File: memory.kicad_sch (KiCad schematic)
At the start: 4 parts, among them U8 62256, U9 KM28C64A

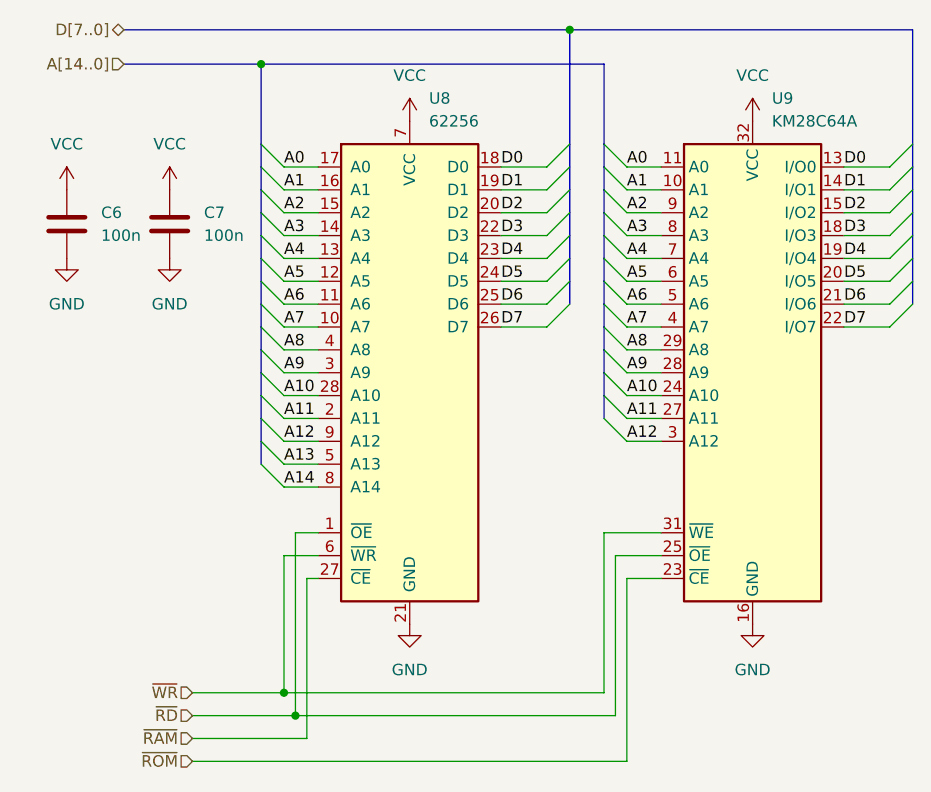
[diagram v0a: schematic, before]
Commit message: HW: Initial placement of I/O chips
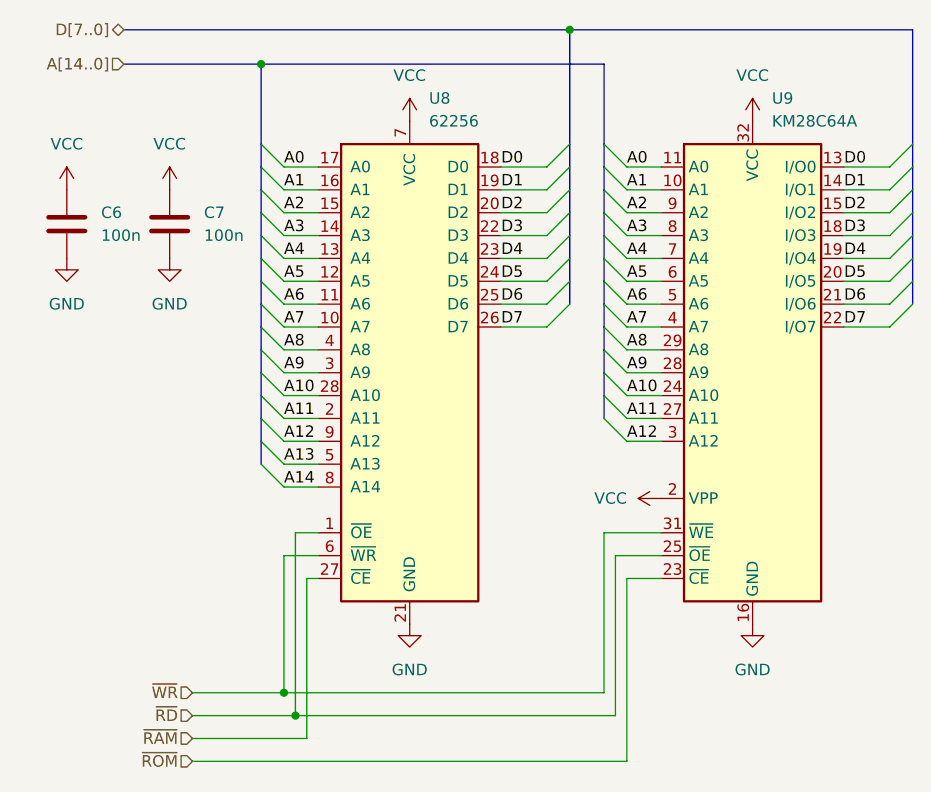
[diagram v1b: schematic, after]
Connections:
- net VCC: now also U9.2 (VPP)
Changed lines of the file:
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@@
+	)
+	(symbol
+		(lib_id "power:VCC")
+		(at 121.92 71.12 90)
+		(unit 1)
+		(exclude_from_sim no)
+		(in_bom yes)
+		(on_board yes)
+		(dnp no)
+		(fields_autoplaced yes)
+		(property "Reference" "#PWR054"
+			(at 125.73 71.12 0)
+			(effects
+				(font
+					(size 1.27 1.27)
+				)
+				(hide yes)
+			)
+		)
+		(property "Value" "VCC"
+			(at 118.11 71.1199 90)
+			(effects
+				(font
+					(size 1.27 1.27)
+				)
+				(justify left)
+			)
+		)
+		(property "Footprint" ""
+			(at 121.92 71.12 0)
+			(effects
+				(font
+					(size 1.27 1.27)
+				)
+				(hide yes)
+			)
+		)
+		(property "Datasheet" ""
+			(at 121.92 71.12 0)
+			(effects
+				(font
+					(size 1.27 1.27)
+				)
+				(hide yes)
+			)
+		)
+		(property "Description" "Power symbol creates a global label with name \"VCC\""
+			(at 121.92 71.12 0)
+			(effects
+				(font
+					(size 1.27 1.27)
+				)
+				(hide yes)
+			)
+		)
+		(pin "1"
+		)
+		(instances
+			(project "pocket80"
+				(path "/328c075d-c706-4d2d-bd37-a88a0c604482/6fedc853-a726-478a-9af0-d8a49315d8a8"
+					(reference "#PWR054")
+					(unit 1)
+				)
+			)
+		)
 	)
 	(symbol
@@
 		(pin "13"
 		)
-		(pin "1"
+		(pin "2"
 		)
 		(pin "24"

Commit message: HW: Update schematic info frames
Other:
- company: (none) -> A.K.
- title: (none) -> Memory
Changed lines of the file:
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@@
 	(generator_version "9.0")
 	(paper "A5")
+	(title_block
+		(title "Memory")
+		(date "2025-10-14")
+		(rev "A")
+		(company "A.K.")
+	)
 	(junction
 		(at 77.47 22.86)

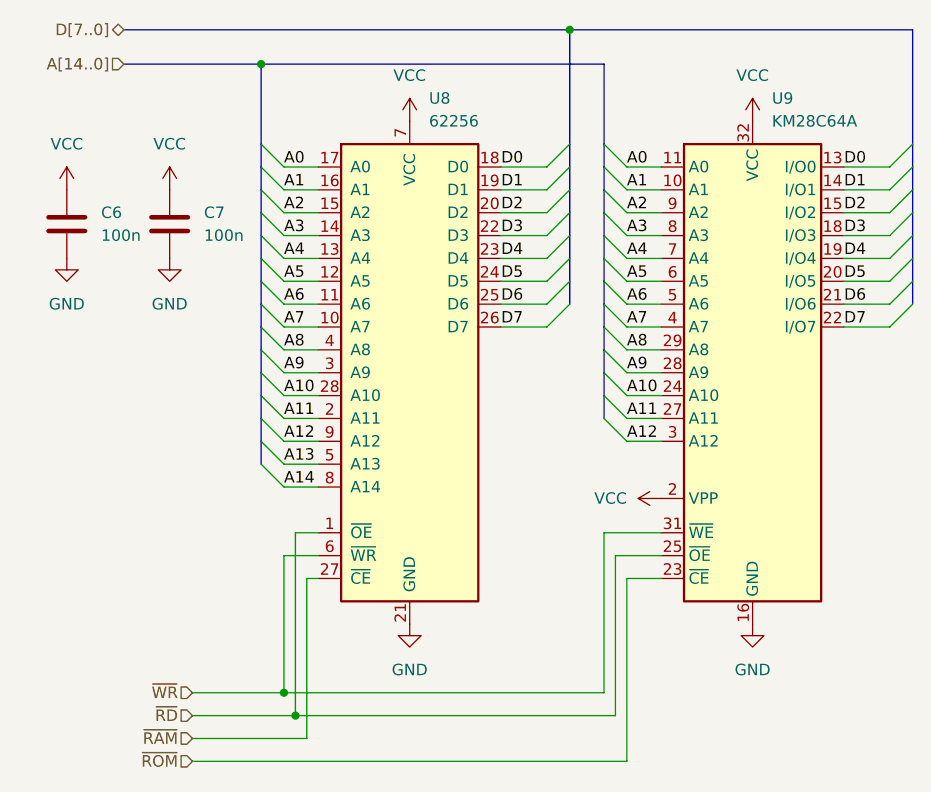
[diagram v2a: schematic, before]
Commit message: HW: Replace 28C64/27C64 EEPROM with 28C256
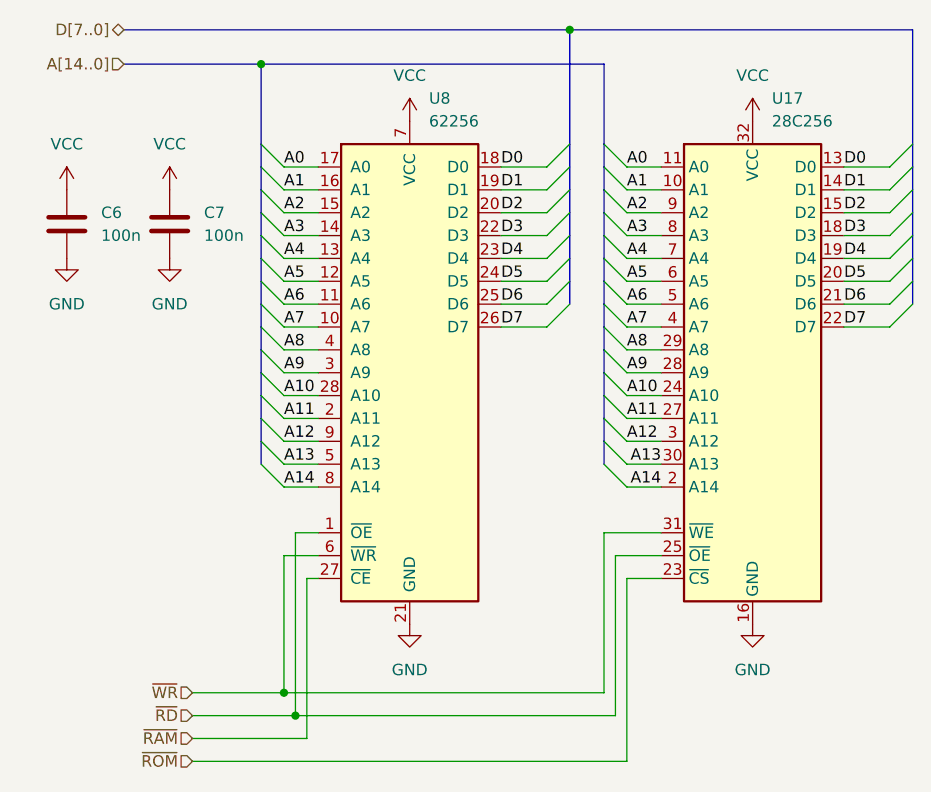
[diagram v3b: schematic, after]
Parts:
- removed U9: KM28C64A, Package_LCC:PLCC-32_11.4x14.0mm_P1.27mm, symbol Memory_EEPROM:KM28C64A
- added U17: 28C256, Package_LCC:PLCC-32_11.4x14.0mm_P1.27mm, symbol Memory_EEPROM:28C256
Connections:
- net A0: now also U17.11 (A0)
- net A1: now also U17.10 (A1)
- net A10: now also U17.24 (A10)
- net A11: now also U17.27 (A11)
- net A12: now also U17.3 (A12)
- net A13: now also U17.30 (A13)
- net A14: now also U17.2 (A14)
- net A2: now also U17.9 (A2)
- net A3: now also U17.8 (A3)
- net A4: now also U17.7 (A4)
- net A5: now also U17.6 (A5)
- net A6: now also U17.5 (A6)
- net A7: now also U17.4 (A7)
- net A8: now also U17.29 (A8)
- net A9: now also U17.28 (A9)
- net D0: now also U17.13 (D0)
- net D1: now also U17.14 (D1)
- net D2: now also U17.15 (D2)
- net D3: now also U17.18 (D3)
- net D4: now also U17.19 (D4)
- net D5: now also U17.20 (D5)
- net D6: now also U17.21 (D6)
- net D7: now also U17.22 (D7)
- net GND: now also U17.16 (GND)
- net VCC: now also U17.32 (VCC)
- net ~{RD}: now also U17.25 (~{OE})
- net ~{ROM}: now also U17.23 (~{CS})
- net ~{WR}: now also U17.31 (~{WE})
